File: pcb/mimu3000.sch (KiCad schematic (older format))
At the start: 16 parts, among them J1 OPT, SW1 ONOFF, U1 AQY211EH, U2 ATTINY88AU

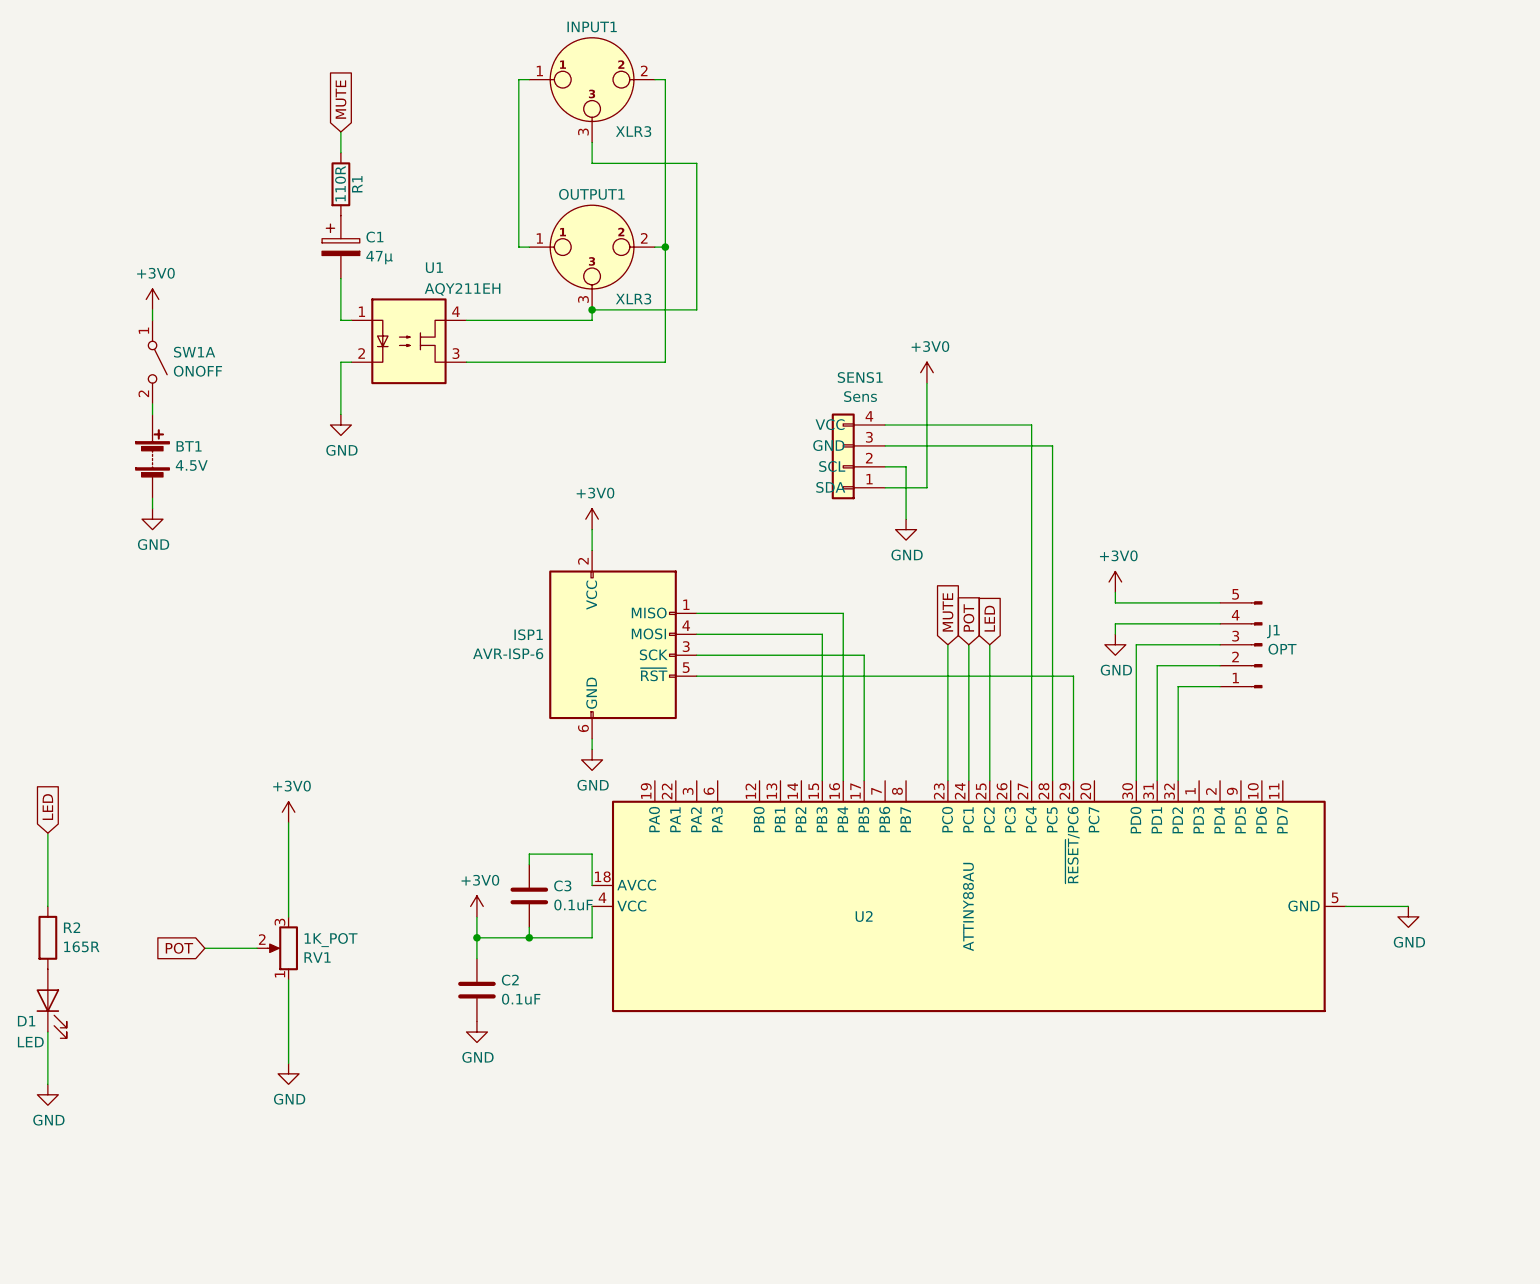
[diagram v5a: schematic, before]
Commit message: Switched to 3xAAA container, Vertically fixed Sensor and the possibility to adding a tantal for de-pop
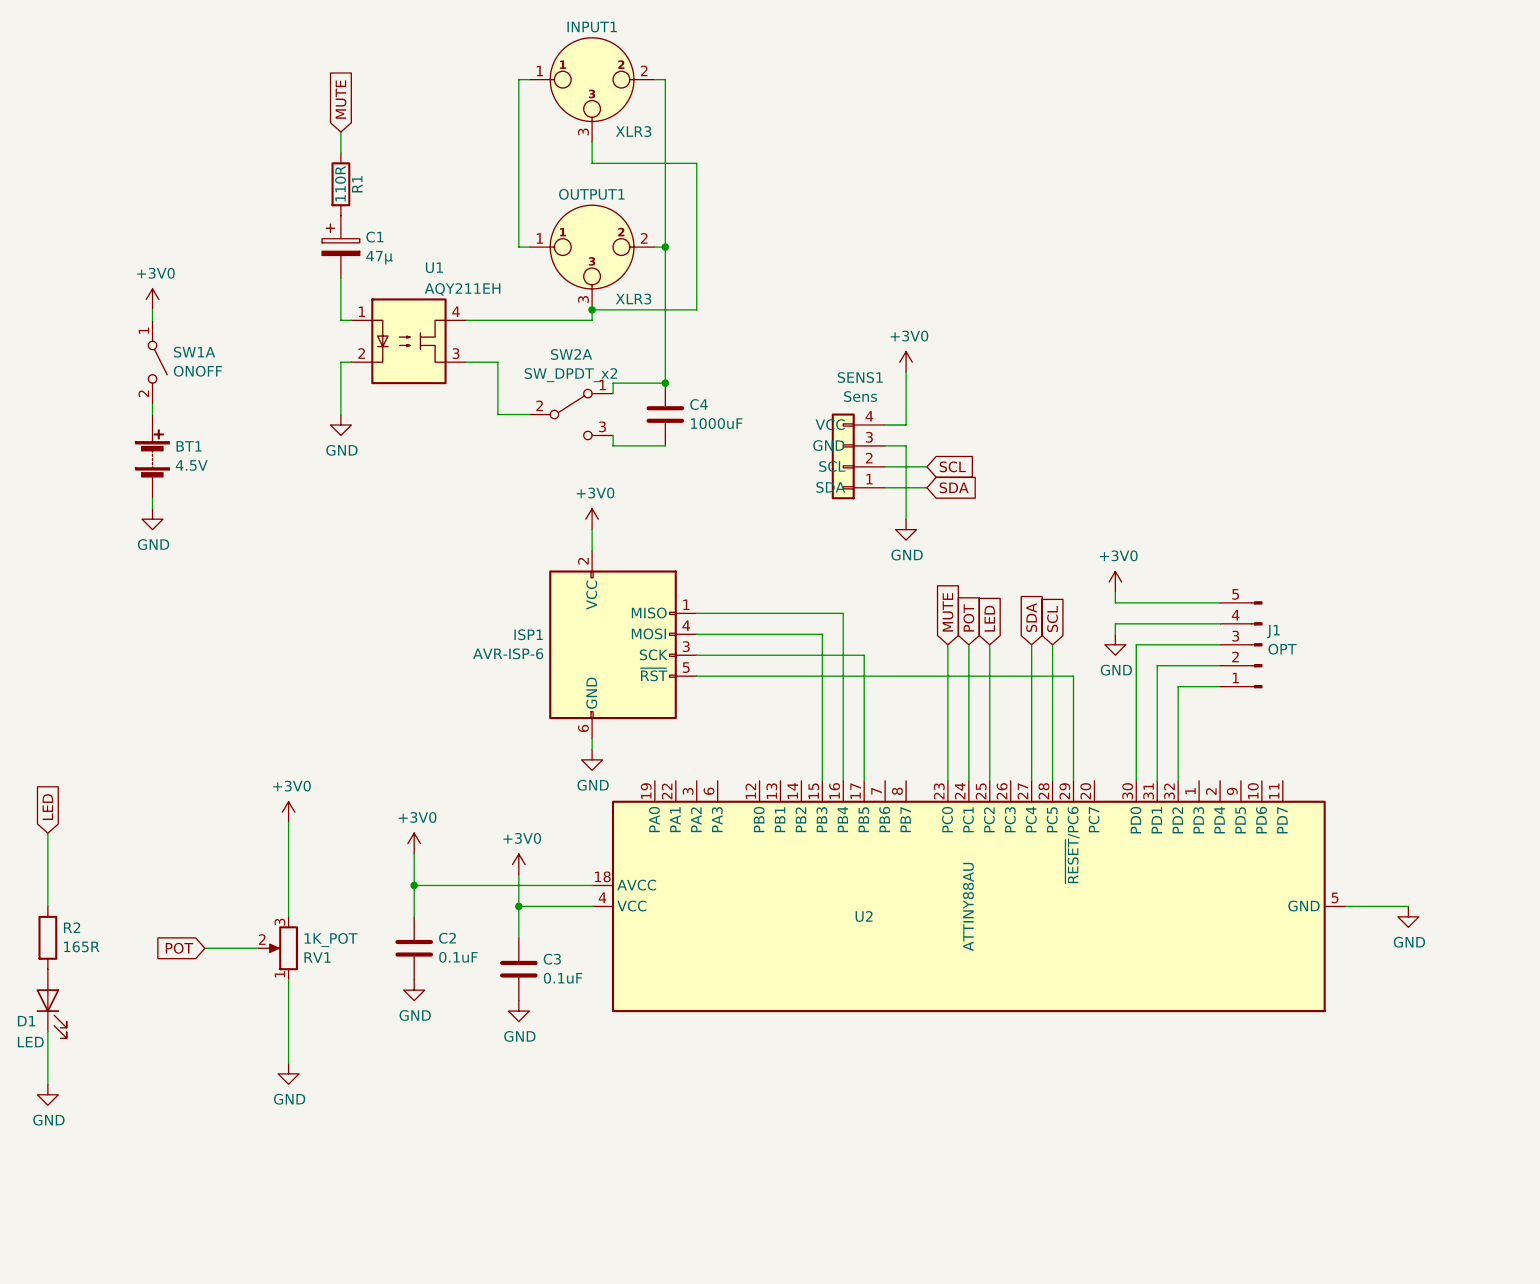
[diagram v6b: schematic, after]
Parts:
- added C4: 1000uF, Capacitor_Tantalum_SMD:CP_EIA-7343-15_Kemet-W, symbol Device:C
- added SW2: SW_DPDT_x2, Jumper:SolderJumper-3_P1.3mm_Bridged12_RoundedPad1.0x1.5mm, symbol Switch:SW_DPDT_x2
- BT1: footprint Battery_Holders:Keystone_2468_2xAAA -> custom:BatteryHolder_Generic_3xAAA
- SENS1: footprint Connector_JST:JST_EH_B4B-EH-A_1x04_P2.50mm_Vertical -> Connector_PinHeader_2.00mm:PinHeader_1x04_P2.00mm_Horizontal
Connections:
- net +3V0: now also C3.1, SENS1.4 (VCC), U2.18 (AVCC); no longer C3.2, SENS1.1 (SDA)
- net GND: now also C3.2, SENS1.3 (GND); no longer SENS1.2 (SCL)
- net SDA: now reaches U2.27 (PC4)
- net SDA: now also SENS1.1 (SDA); no longer SENS1.4 (VCC)
- net SCL: now reaches U2.28 (PC5)
- net SCL: now also SENS1.2 (SCL); no longer SENS1.3 (GND)
- net at INPUT1.2, OUTPUT1.2: now also C4.1, SW2.1 (A); no longer U1.3
- new net: SW2.2 (B), U1.3
- new net: C4.2, SW2.3 (C)
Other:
- moved on the sheet: C2, C3

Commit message: Use electrolyte caps
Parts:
- added C5: 1000uF, Capacitor_THT:CP_Radial_D8.0mm_P3.50mm, symbol Device:CP
- C4: footprint Capacitor_Tantalum_SMD:CP_EIA-7343-15_Kemet-W -> Capacitor_THT:CP_Radial_D8.0mm_P3.50mm; symbol Device:C -> Device:CP
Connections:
- net at C4.1, INPUT1.2, OUTPUT1.2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: now also C5.2
- net at C4.2, SW2.3 (C): now also C5.1
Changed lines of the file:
@@
 Connection ~ 5500 2750
 $Comp
-L Device:C C4
+L Device:CP C4
 U 1 1 5E4B8635
 P 5500 2900
-F 0 "C4" H 5615 2946 50  0000 L CNN
-F 1 "1000uF" H 5615 2855 50  0000 L CNN
-F 2 "Capacitor_Tantalum_SMD:CP_EIA-7343-15_Kemet-W" H 5538 2750 50  0001 C CNN
+F 0 "C4" H 5600 2950 50  0000 L CNN
+F 1 "1000uF" H 5350 2650 50  0000 L CNN
+F 2 "Capacitor_THT:CP_Radial_D8.0mm_P3.50mm" H 5538 2750 50  0001 C CNN
 F 3 "~" H 5500 2900 50  0001 C CNN
 	1    5500 2900
@@
 	4300 5000 4300 5150
 $Comp
-L power:GND #PWR?
+L power:GND #PWR0104
 U 1 1 5E50B04B
 P 4800 5700
-F 0 "#PWR?" H 4800 5450 50  0001 C CNN
+F 0 "#PWR0104" H 4800 5450 50  0001 C CNN
 F 1 "GND" H 4805 5527 50  0000 C CNN
 F 2 "" H 4800 5700 50  0001 C CNN
@@
 $EndComp
 $Comp
-L power:+3V0 #PWR?
+L power:+3V0 #PWR0105
 U 1 1 5E50B347
 P 4800 5100
-F 0 "#PWR?" H 4800 4950 50  0001 C CNN
+F 0 "#PWR0105" H 4800 4950 50  0001 C CNN
 F 1 "+3V0" H 4815 5273 50  0000 C CNN
 F 2 "" H 4800 5100 50  0001 C CNN
@@
 Wire Wire Line
 	4300 5150 4300 5300
+$Comp
+L Device:CP C5
+U 1 1 5E4AE3C7
+P 5800 2900
+F 0 "C5" H 5600 2850 50  0000 L CNN
+F 1 "1000uF" H 5650 3150 50  0000 L CNN
+F 2 "Capacitor_THT:CP_Radial_D8.0mm_P3.50mm" H 5838 2750 50  0001 C CNN
+F 3 "~" H 5800 2900 50  0001 C CNN
+	1    5800 2900
+	-1   0    0    1
+$EndComp
+Wire Wire Line
+	5800 2750 5500 2750
+Wire Wire Line
+	5500 3050 5800 3050
+Connection ~ 5500 3050
 $EndSCHEMATC

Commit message: Flipped Sensor to save space
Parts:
- SENS1: symbol custom:Conn_TOF -> custom:Conn_TOF_flipped
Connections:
- net +3V0: now also SENS1.1 (VCC); no longer SENS1.4 (VCC)
- net GND: now also SENS1.2 (GND); no longer SENS1.3 (GND)
- net SCL: now also SENS1.3 (SCL); no longer SENS1.2 (SCL)
- net SDA: now also SENS1.4 (SDA); no longer SENS1.1 (SDA)
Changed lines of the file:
@@
 $EndComp
 $Comp
-L custom:Conn_TOF SENS1
+L custom:Conn_TOF_flipped SENS1
 U 1 1 5E2CBB84
 P 6350 3150
@@
 	1    0    0    -1
 $EndComp
-Wire Wire Line
-	6650 2700 6650 2950
 $Comp
 L power:GND #PWR011
@@
 Wire Wire Line
 	7350 4000 7350 4650
-Text GLabel 6750 3250 2    50   Input ~ 0
+Text GLabel 6850 2950 2    50   Input ~ 0
 SDA
-Text GLabel 6750 3150 2    50   Input ~ 0
+Text GLabel 6850 3050 2    50   Input ~ 0
 SCL
 $Comp
 L power:GND #PWR04
 U 1 1 5E434EA3
-P 6650 3400
-F 0 "#PWR04" H 6650 3150 50  0001 C CNN
-F 1 "GND" H 6655 3227 50  0000 C CNN
-F 2 "" H 6650 3400 50  0001 C CNN
-F 3 "" H 6650 3400 50  0001 C CNN
-	1    6650 3400
-	1    0    0    -1
-$EndComp
-Wire Wire Line
-	6550 2950 6650 2950
-Wire Wire Line
-	6550 3050 6650 3050
-Wire Wire Line
-	6650 3050 6650 3400
-Wire Wire Line
-	6550 3250 6750 3250
-Wire Wire Line
-	6750 3150 6550 3150
+P 6750 3400
+F 0 "#PWR04" H 6750 3150 50  0001 C CNN
+F 1 "GND" H 6755 3227 50  0000 C CNN
+F 2 "" H 6750 3400 50  0001 C CNN
+F 3 "" H 6750 3400 50  0001 C CNN
+	1    6750 3400
+	1    0    0    -1
+$EndComp
 $Comp
 L Switch:SW_DPDT_x2 SW2
@@
 	5500 3050 5800 3050
 Connection ~ 5500 3050
+Wire Wire Line
+	6650 3250 6550 3250
+Wire Wire Line
+	6650 2700 6650 3250
+Wire Wire Line
+	6750 3400 6750 3150
+Wire Wire Line
+	6750 3150 6550 3150
+Wire Wire Line
+	6550 3050 6850 3050
+Wire Wire Line
+	6850 2950 6550 2950
 $EndSCHEMATC
